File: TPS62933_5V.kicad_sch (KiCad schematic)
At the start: 20 parts

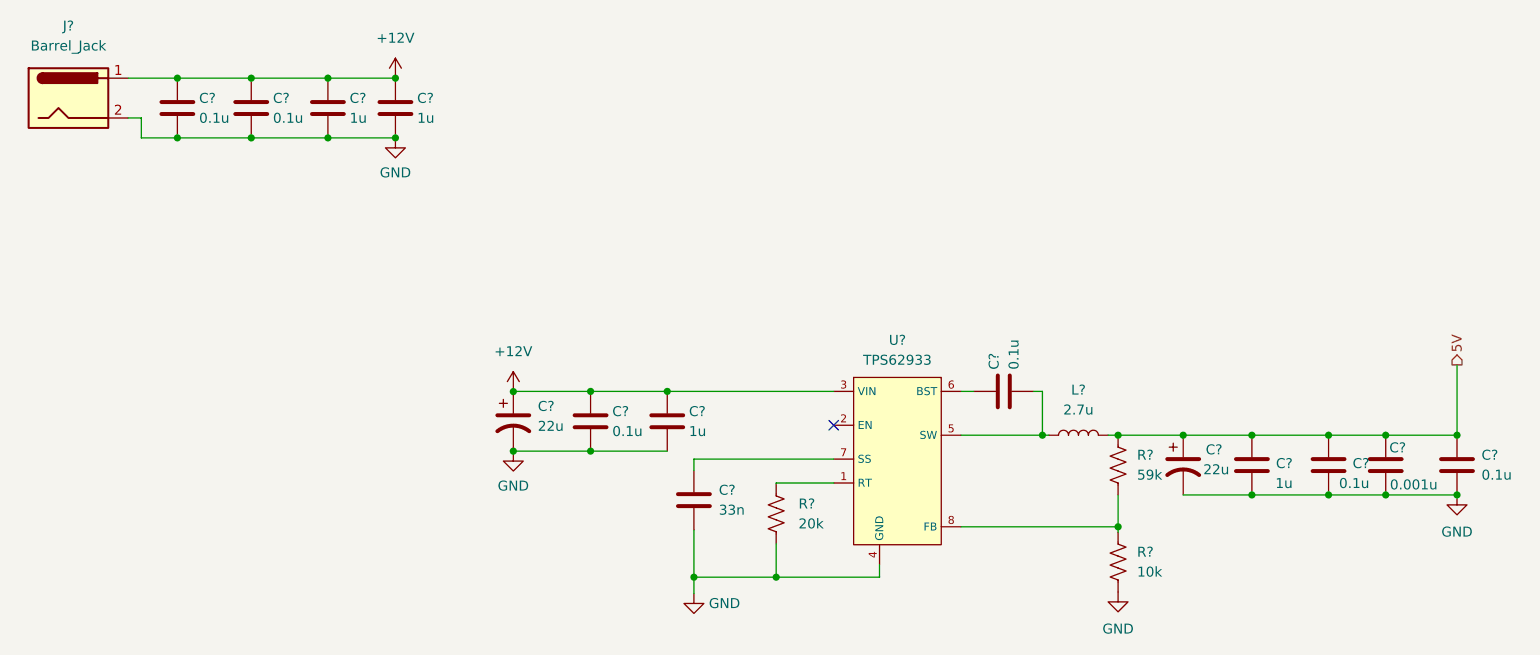
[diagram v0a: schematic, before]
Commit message: fixing sheet numbers and adding schematic PDF
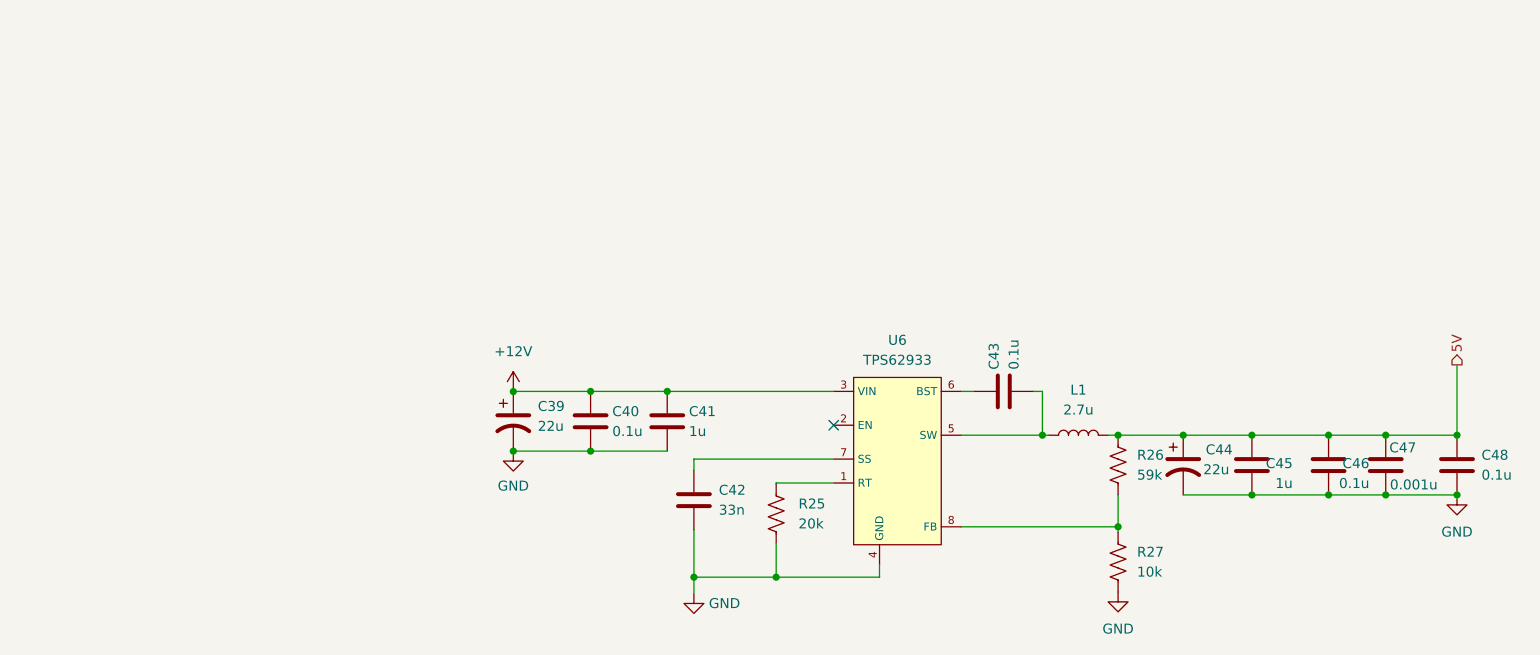
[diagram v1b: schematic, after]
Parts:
- removed C? (x2): 1u, symbol Device:C
- removed C? (x2): 0.1u, symbol Device:C
- removed J?: Barrel_Jack, symbol Connector:Barrel_Jack
- gave numbers to parts that had none: 15

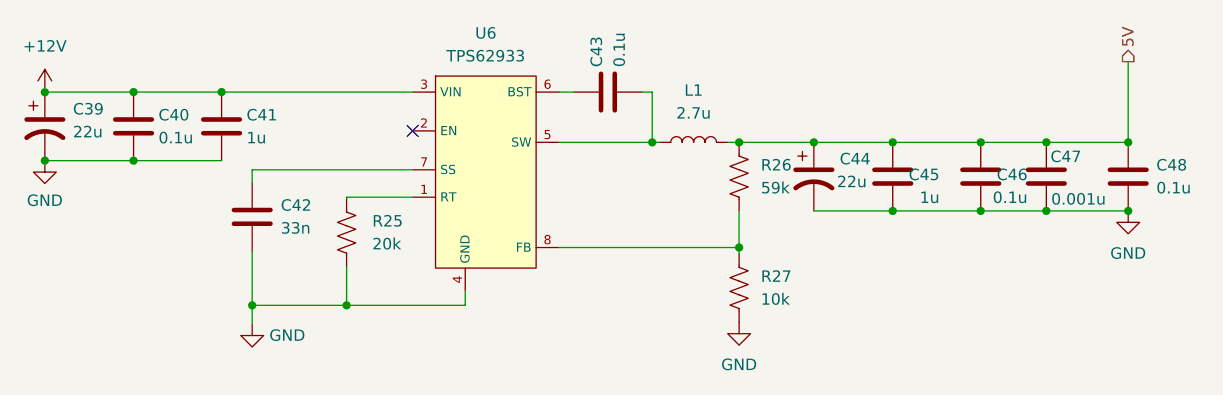
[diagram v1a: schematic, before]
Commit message: Fixing ERC
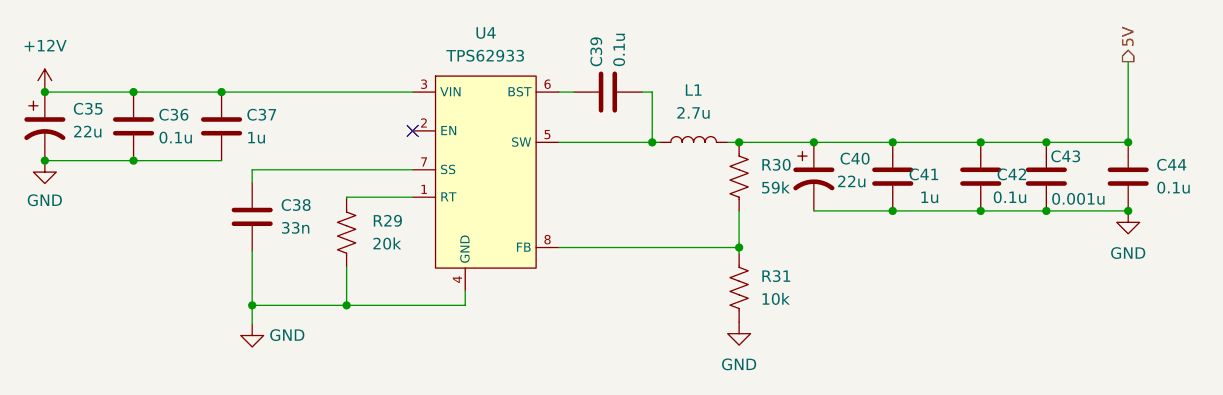
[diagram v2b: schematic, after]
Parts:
- renumbered C39 to C35, C40 to C36, C41 to C37, C42 to C38, C43 to C39, C44 to C40, C45 to C41, C46 to C42, C47 to C43, C48 to C44, R25 to R29, R26 to R30, R27 to R31, U6 to U4
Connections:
- net +12V: now also C35.1, C36.1, C37.1, U4.3 (VIN)
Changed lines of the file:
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@@
 (kicad_sch (version 20211123) (generator eeschema)
   (paper "A4")
+  (junction (at 93.1672 80.1878) (diameter 0) (color 0 0 0 0)
+  )
   (junction (at 116.205 103.886) (diameter 0) (color 0 0 0 0)
   )
   (junction (at 178.6128 85.7758) (diameter 0) (color 0 0 0 0)
-  )
-  (junction (at 93.1672 80.2132) (diameter 0) (color 0 0 0 0)
   )
   (junction (at 197.1548 85.7758) (diameter 0) (color 0 0 0 0)
@@
   (symbol (lib_id "Device:R_US") (at 170.307 89.5858 0) (unit 1)
     (in_bom yes) (on_board yes) (fields_autoplaced)
-    (property "Reference" "R26" (id 0) (at 172.72 88.3157 0)
+    (property "Reference" "R30" (id 0) (at 172.72 88.3157 0)
       (effects (font (size 1.27 1.27)) (justify left))
     )
@@
   (symbol (lib_id "Power:TPS62933") (at 142.6718 88.5698 0) (unit 1)
     (in_bom yes) (on_board yes) (fields_autoplaced)
-    (property "Reference" "U6" (id 0) (at 142.1638 73.66 0))
+    (property "Reference" "U4" (id 0) (at 142.1638 73.66 0))
     (property "Value" "TPS62933" (id 1) (at 142.1638 76.2 0))
     (property "Footprint" "" (id 2) (at 142.9258 105.0798 0)
@@
   (symbol (lib_id "Device:C") (at 187.3758 89.5858 0) (mirror y) (unit 1)
     (in_bom yes) (on_board yes)
-    (property "Reference" "C45" (id 0) (at 192.5828 89.3826 0)
+    (property "Reference" "C41" (id 0) (at 192.5828 89.3826 0)
       (effects (font (size 1.27 1.27)) (justify left))
     )
@@
     (pin "2")
   )
-  (symbol (lib_id "power:+12V") (at 93.1672 80.2132 0) (unit 1)
-    (in_bom yes) (on_board yes) (fields_autoplaced)
-    (property "Reference" "#PWR061" (id 0) (at 93.1672 84.0232 0)
-      (effects (font (size 1.27 1.27)) hide)
-    )
-    (property "Value" "+12V" (id 1) (at 93.1672 75.1078 0))
-    (property "Footprint" "" (id 2) (at 93.1672 80.2132 0)
-      (effects (font (size 1.27 1.27)) hide)
-    )
-    (property "Datasheet" "" (id 3) (at 93.1672 80.2132 0)
+  (symbol (lib_id "power:+12V") (at 93.1672 80.1878 0) (unit 1)
+    (in_bom yes) (on_board yes) (fields_autoplaced)
+    (property "Reference" "#PWR059" (id 0) (at 93.1672 83.9978 0)
+      (effects (font (size 1.27 1.27)) hide)
+    )
+    (property "Value" "+12V" (id 1) (at 93.1672 75.0824 0))
+    (property "Footprint" "" (id 2) (at 93.1672 80.1878 0)
+      (effects (font (size 1.27 1.27)) hide)
+    )
+    (property "Datasheet" "" (id 3) (at 93.1672 80.1878 0)
       (effects (font (size 1.27 1.27)) hide)
     )
@@
   (symbol (lib_id "Device:C") (at 213.5378 89.5858 0) (unit 1)
     (in_bom yes) (on_board yes) (fields_autoplaced)
-    (property "Reference" "C48" (id 0) (at 216.662 88.3157 0)
+    (property "Reference" "C44" (id 0) (at 216.662 88.3157 0)
       (effects (font (size 1.27 1.27)) (justify left))
     )
@@
   (symbol (lib_id "Device:C") (at 197.1548 89.5858 0) (mirror y) (unit 1)
     (in_bom yes) (on_board yes)
-    (property "Reference" "C46" (id 0) (at 202.3618 89.3826 0)
+    (property "Reference" "C42" (id 0) (at 202.3618 89.3826 0)
       (effects (font (size 1.27 1.27)) (justify left))
     )
@@
   (symbol (lib_id "Device:C") (at 155.7274 80.1878 90) (unit 1)
     (in_bom yes) (on_board yes)
-    (property "Reference" "C43" (id 0) (at 154.4828 77.4192 0)
+    (property "Reference" "C39" (id 0) (at 154.4828 77.4192 0)
       (effects (font (size 1.27 1.27)) (justify left))
     )
@@
   (symbol (lib_id "Device:R_US") (at 170.307 101.9556 0) (unit 1)
     (in_bom yes) (on_board yes) (fields_autoplaced)
-    (property "Reference" "R27" (id 0) (at 172.72 100.6855 0)
+    (property "Reference" "R31" (id 0) (at 172.72 100.6855 0)
       (effects (font (size 1.27 1.27)) (justify left))
     )
@@
   (symbol (lib_id "Device:C_Polarized_US") (at 93.1672 83.9978 0) (unit 1)
     (in_bom yes) (on_board yes) (fields_autoplaced)
-    (property "Reference" "C39" (id 0) (at 96.2914 82.0927 0)
+    (property "Reference" "C35" (id 0) (at 96.2914 82.0927 0)
       (effects (font (size 1.27 1.27)) (justify left))
     )
@@
   (symbol (lib_id "power:GND") (at 116.205 105.9688 0) (unit 1)
     (in_bom yes) (on_board yes) (fields_autoplaced)
-    (property "Reference" "#PWR063" (id 0) (at 116.205 112.3188 0)
+    (property "Reference" "#PWR061" (id 0) (at 116.205 112.3188 0)
       (effects (font (size 1.27 1.27)) hide)
     )
@@
   (symbol (lib_id "Device:R_US") (at 126.6952 95.8088 0) (unit 1)
     (in_bom yes) (on_board yes) (fields_autoplaced)
-    (property "Reference" "R25" (id 0) (at 129.54 94.5387 0)
+    (property "Reference" "R29" (id 0) (at 129.54 94.5387 0)
       (effects (font (size 1.27 1.27)) (justify left))
     )
@@
   (symbol (lib_id "Device:C") (at 103.0224 83.9978 0) (unit 1)
     (in_bom yes) (on_board yes)
-    (property "Reference" "C40" (id 0) (at 105.791 82.7532 0)
+    (property "Reference" "C36" (id 0) (at 105.791 82.7532 0)
       (effects (font (size 1.27 1.27)) (justify left))
     )
@@
   (symbol (lib_id "power:GND") (at 170.307 105.7656 0) (unit 1)
     (in_bom yes) (on_board yes) (fields_autoplaced)
-    (property "Reference" "#PWR064" (id 0) (at 170.307 112.1156 0)
+    (property "Reference" "#PWR062" (id 0) (at 170.307 112.1156 0)
       (effects (font (size 1.27 1.27)) hide)
     )
@@
   (symbol (lib_id "power:GND") (at 213.5378 93.3958 0) (unit 1)
     (in_bom yes) (on_board yes) (fields_autoplaced)
-    (property "Reference" "#PWR065" (id 0) (at 213.5378 99.7458 0)
+    (property "Reference" "#PWR063" (id 0) (at 213.5378 99.7458 0)
       (effects (font (size 1.27 1.27)) hide)
     )
@@
   (symbol (lib_id "Device:C") (at 204.4446 89.5858 0) (unit 1)
     (in_bom yes) (on_board yes)
-    (property "Reference" "C47" (id 0) (at 204.9018 87.376 0)
+    (property "Reference" "C43" (id 0) (at 204.9018 87.376 0)
       (effects (font (size 1.27 1.27)) (justify left))
     )
@@
   (symbol (lib_id "Device:C_Polarized_US") (at 178.6128 89.5858 0) (unit 1)
     (in_bom yes) (on_board yes)
-    (property "Reference" "C44" (id 0) (at 181.483 87.63 0)
+    (property "Reference" "C40" (id 0) (at 181.483 87.63 0)
       (effects (font (size 1.27 1.27)) (justify left))
     )
@@
   (symbol (lib_id "power:GND") (at 93.1672 87.8078 0) (unit 1)
     (in_bom yes) (on_board yes) (fields_autoplaced)
-    (property "Reference" "#PWR062" (id 0) (at 93.1672 94.1578 0)
+    (property "Reference" "#PWR060" (id 0) (at 93.1672 94.1578 0)
       (effects (font (size 1.27 1.27)) hide)
     )
@@
   (symbol (lib_id "Device:C") (at 116.205 94.0562 0) (unit 1)
     (in_bom yes) (on_board yes) (fields_autoplaced)
-    (property "Reference" "C42" (id 0) (at 119.38 92.7861 0)
+    (property "Reference" "C38" (id 0) (at 119.38 92.7861 0)
       (effects (font (size 1.27 1.27)) (justify left))
     )
@@
   (symbol (lib_id "Device:C") (at 112.8014 83.9978 0) (unit 1)
     (in_bom yes) (on_board yes)
-    (property "Reference" "C41" (id 0) (at 115.57 82.7532 0)
-      (effects (font (size 1.27 1.27)) (justify left))
-    )
+    (property "Reference" "C37" (id 0) (at 115.57 82.7532 0)
+      (effects (font (size 1.27 1.27)) (justify left))
+    )

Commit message: Pushing what i have now
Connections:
- net 5V renamed +5V
